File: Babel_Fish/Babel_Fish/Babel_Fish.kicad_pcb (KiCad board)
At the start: 4 copper layers, 50 x 50 mm, 85 parts, among them J1 USB_C_Receptacle_USB2.0, J2 U.FL, J3 Conn_01x08, J4 Conn_01x02, Q1 Q_NMOS_GSD, SW2 SLIDE, U1 MCU_RaspberryPi_RP2040_RP2040, U10 WE_171021801, U2 TVS1800DRVR, U3 USBLC6-2SC6, U4 TPS2121RUXR, U5 W25Q128JVS, U6 LT6703CDC-3, U7 DRF1262TL, U8 MB85RS1MT, U9 WE 171010550, Y1 12MHz

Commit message: started routing Babel Fish
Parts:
- added J5: Conn_01x04, Connector_PinHeader_2.54mm:PinHeader_1x04_P2.54mm_Vertical, F.Cu at (159.6, 132.3)
- moved Y1 135.8 mm to (202.3, 105.0), turned to 90 degrees
- moved R2 120.2 mm to (209.6, 105.5), turned to 90 degrees
- moved C4 105.0 mm to (206.4, 104.2), turned to -90 degrees
- moved C3 103.1 mm to (204.8, 105.7)
- moved J1 102.1 mm to (206.7, 83.5), turned to 180 degrees
- moved C7 100.7 mm to (205.4, 104.2), turned to -90 degrees
- moved C2 99.9 mm to (201.5, 102.7), turned to 180 degrees
- moved B1 98.2 mm to (212.4, 105.6), turned to -90 degrees
- moved R1 97.5 mm to (204.4, 104.2), turned to 90 degrees
- moved TP1 95.6 mm to (206.7, 107.4)
- moved TP2 92.7 mm to (203.7, 108.5)
- moved U4 88.7 mm to (142.5, 63.6)
- moved C24 78.5 mm to (154.7, 81.8)
- moved C39 78.5 mm to (154.7, 85.2)
- moved U6 76.2 mm to (140.1, 75.4)
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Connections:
- U1 pad 28: /EXTINT -> unconnected-(U1-GPIO17-Pad28)
- U1 pad 29: /TIMEPULSE -> unconnected-(U1-GPIO18-Pad29)
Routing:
- net /RP_SWD: track 0.00 -> 15.2 mm
- net /QSPI_SS: track 0.00 -> 15.1 mm
- net /QSPI_SD1: track 0.00 -> 13.7 mm
- net /QSPI_SD2: track 0.00 -> 12.4 mm
- net Net-(U1-RUN): track 0.00 -> 12.3 mm
- net /RP_SWCLK: track 0.00 -> 8.07 mm
- net /QSPI_SD3: track 0.00 -> 6.39 mm
- net /QSPI_SCLK: track 0.00 -> 5.29 mm
- net Net-(U10-FB): track 0.00 -> 4.80 mm
- net Net-(U1-XIN): track 0.00 -> 4.49 mm
- net /QSPI_SD0: track 0.00 -> 4.25 mm
- net Net-(U4-IN2): track 0.00 -> 3.91 mm
- net +1V1: track 0.00 -> 3.77 mm
- net +3V3: track 0.00 -> 3.56 mm
- net Net-(U1-XOUT): track 0.00 -> 2.97 mm
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
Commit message: more Babel fish routing
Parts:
- R3, R4: moved to B.Cu
- moved R3 119.3 mm to (208.0, 83.0), turned to -90 degrees
- moved R4 117.0 mm to (205.0, 83.0), turned to 90 degrees
- moved C1 100.9 mm to (202.0, 95.5), turned to 135 degrees
- moved C11 99.4 mm to (202.7, 94.7), turned to 135 degrees
- moved U3 93.8 mm to (206.7, 90.6), turned to 90 degrees
- moved R6 90.8 mm to (205.6, 96.3), turned to -90 degrees
- moved R5 90.3 mm to (204.6, 96.3), turned to -90 degrees
- moved C9 11.7 mm to (141.5, 57.9)
- moved B1 4.57 mm to (211.6, 110.1)
- moved C2 4.57 mm to (200.7, 107.2)
- moved C3 4.57 mm to (204.0, 110.2)
- moved C4 4.57 mm to (205.6, 108.7)
- moved C7 4.57 mm to (204.6, 108.7)
- moved R1 4.57 mm to (203.6, 108.7)
- moved U1 4.57 mm to (203.3, 102.0)
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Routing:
- net VBUS: track 0.00 -> 11.7 mm
- net GND: track 0.00 -> 10.1 mm, vias 0 -> 1
- net Net-(J1-D--PadA7): track 0.00 -> 5.16 mm
- net /USB_D-: track 0.00 -> 4.91 mm
- net +3V3: track 3.56 -> 8.32 mm
- net /USB_D+: track 0.00 -> 4.56 mm
- net Net-(J1-D+-PadA6): track 0.00 -> 4.43 mm
- net Net-(J1-CC1): track 0.00 -> 3.38 mm, vias 0 -> 1
- net Net-(J1-CC2): track 0.00 -> 3.34 mm, vias 0 -> 1
- net +1V1: track 3.77 -> 6.84 mm

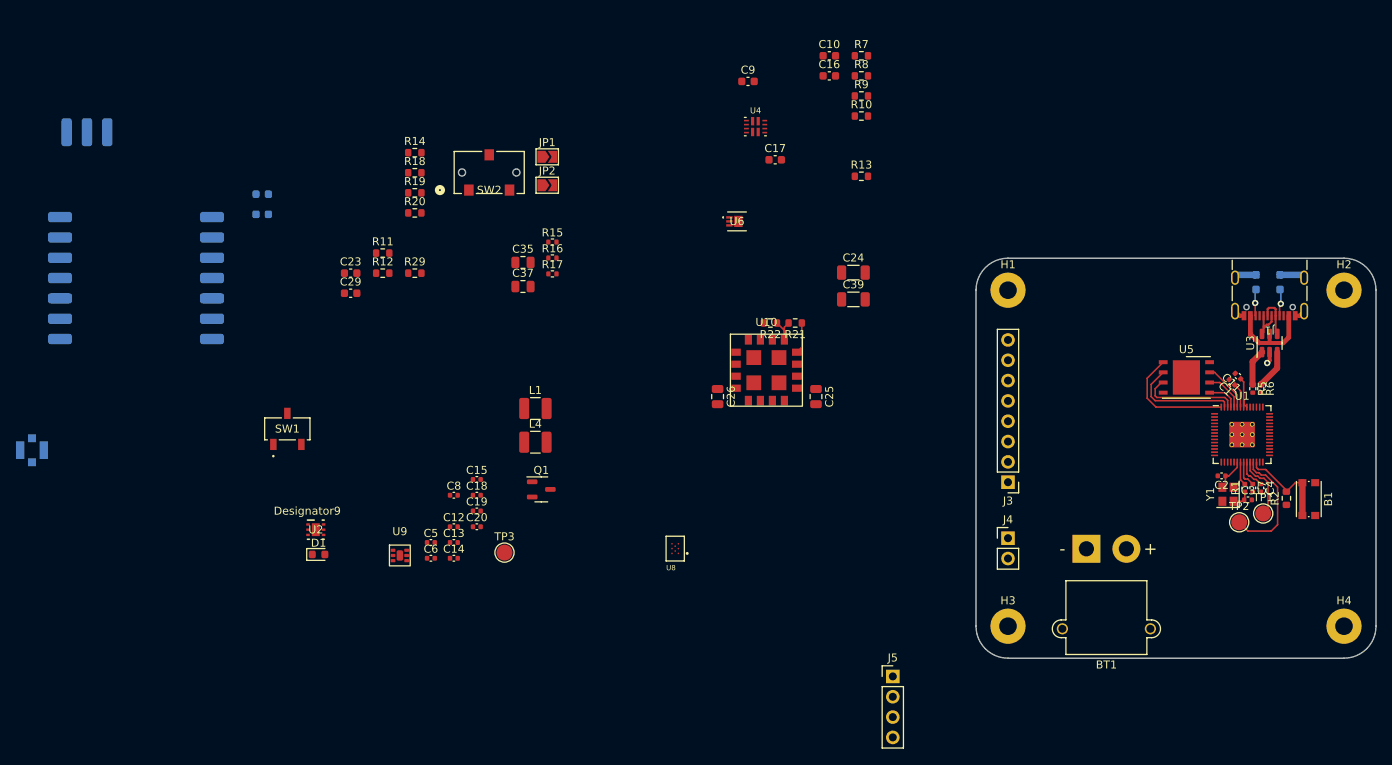
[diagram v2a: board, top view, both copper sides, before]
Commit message: babel fish more routing work
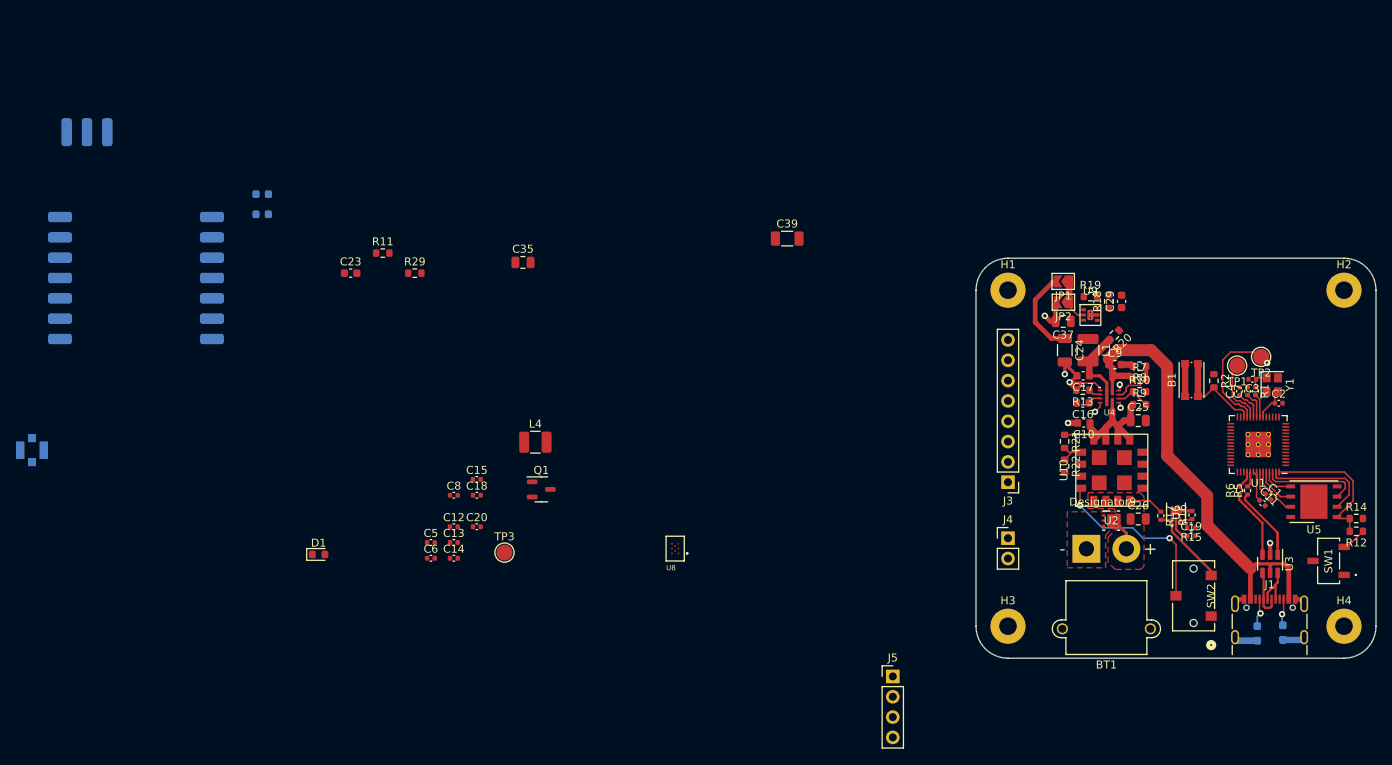
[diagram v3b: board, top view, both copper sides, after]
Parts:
- moved SW1 131.2 mm to (214.1, 117.8), turned to 90 degrees
- moved R14 126.3 mm to (217.5, 112.5)
- moved R12 125.9 mm to (217.5, 114.1), turned to 180 degrees
- moved SW2 102.7 mm to (197.2, 122.2), turned to 90 degrees
- moved U2 99.4 mm to (186.9, 112.8)
- moved C29 96.4 mm to (188.2, 85.4), turned to 90 degrees
- moved U9 91.4 mm to (184.3, 87.1)
- moved C19 89.4 mm to (196.9, 114.7)
- moved R20 88.8 mm to (187.3, 89.6), turned to -135 degrees
- moved R18 88.2 mm to (186.6, 85.4), turned to 90 degrees
- moved R15 87.5 mm to (196.9, 113.7), turned to 180 degrees
- moved R16 86.2 mm to (197.0, 112.1), turned to 90 degrees
- moved R19 85.4 mm to (184.3, 84.8)
- moved R17 81.8 mm to (193.1, 112.2), turned to -90 degrees
- moved L1 69.5 mm to (184.0, 91.5), turned to -90 degrees
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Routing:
- net VBUS: track 11.7 -> 59.5 mm
- net GND: track 10.1 -> 38.8 mm, vias 1 -> 8
- net /CUTOFF: track 0.00 -> 22.7 mm, vias 0 -> 2
- net Net-(U4-IN2): track 3.91 -> 24.1 mm
- net +BATT: track 0.00 -> 11.9 mm
- net +5V: track 0.00 -> 11.1 mm
- net Net-(C17-Pad1): track 0.00 -> 10.6 mm
- net Net-(SW2-C): track 0.00 -> 10.4 mm
- net /USB_D+: track 4.56 -> 11.0 mm
- net Net-(U4-OV1): track 0.00 -> 6.09 mm
- net Net-(JP1-A): track 0.00 -> 5.40 mm
- net Net-(U4-OV2): track 0.00 -> 4.46 mm
- net /USB_D-: track 4.91 -> 8.74 mm
- net /QSPI_SS: track 15.1 -> 18.0 mm
- net Net-(SW1-B): track 0.00 -> 2.76 mm
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- added copper zone on F.Cu, net +BATT
- added copper zone on F.Cu, net GND
